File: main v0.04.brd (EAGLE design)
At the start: 77.5 x 67.3 mm, 70 parts, among them IC1 4050D, U1 MCP73831, U2 TPS61200, U3 MAX1704X, U4 USD-SOCKETNEW, X1 USB-MICROB, Y1 16MHz KX-7

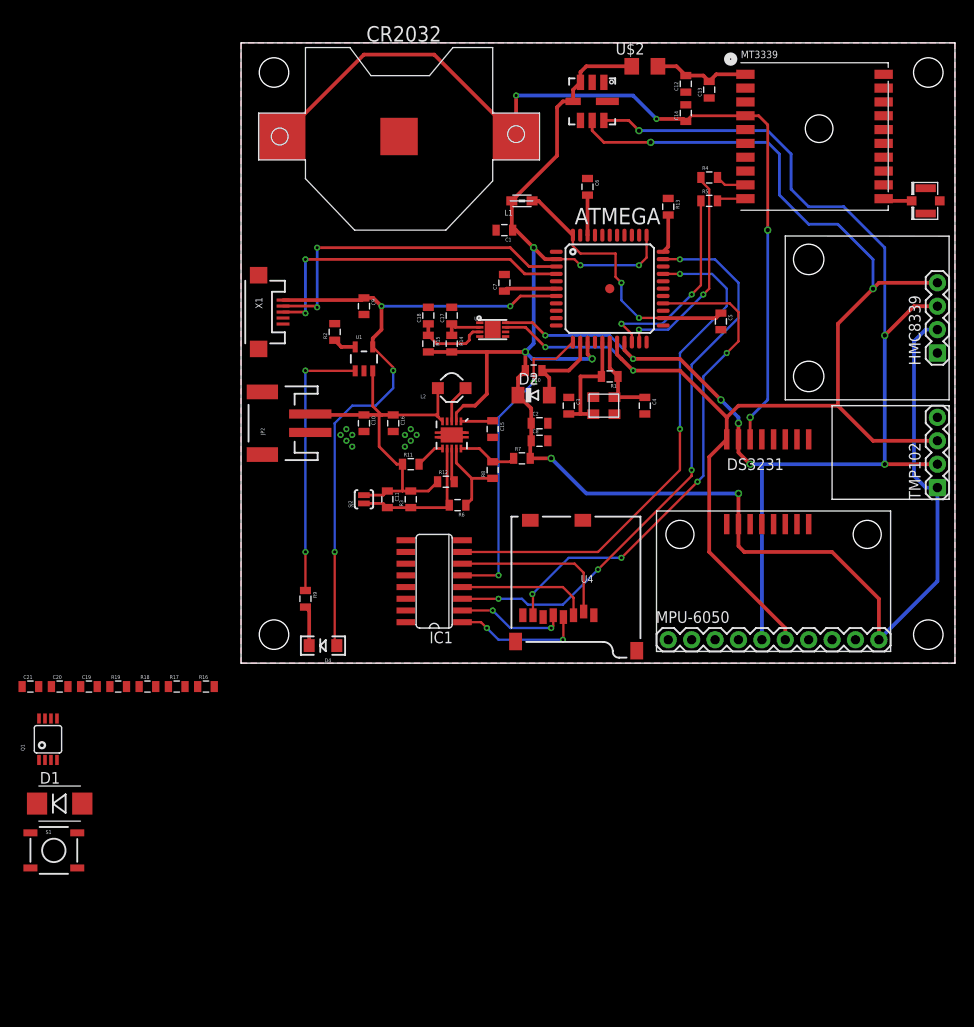
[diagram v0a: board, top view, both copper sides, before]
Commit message: Clean up of schematics
General clean up + 5V reg added + On/off control connected
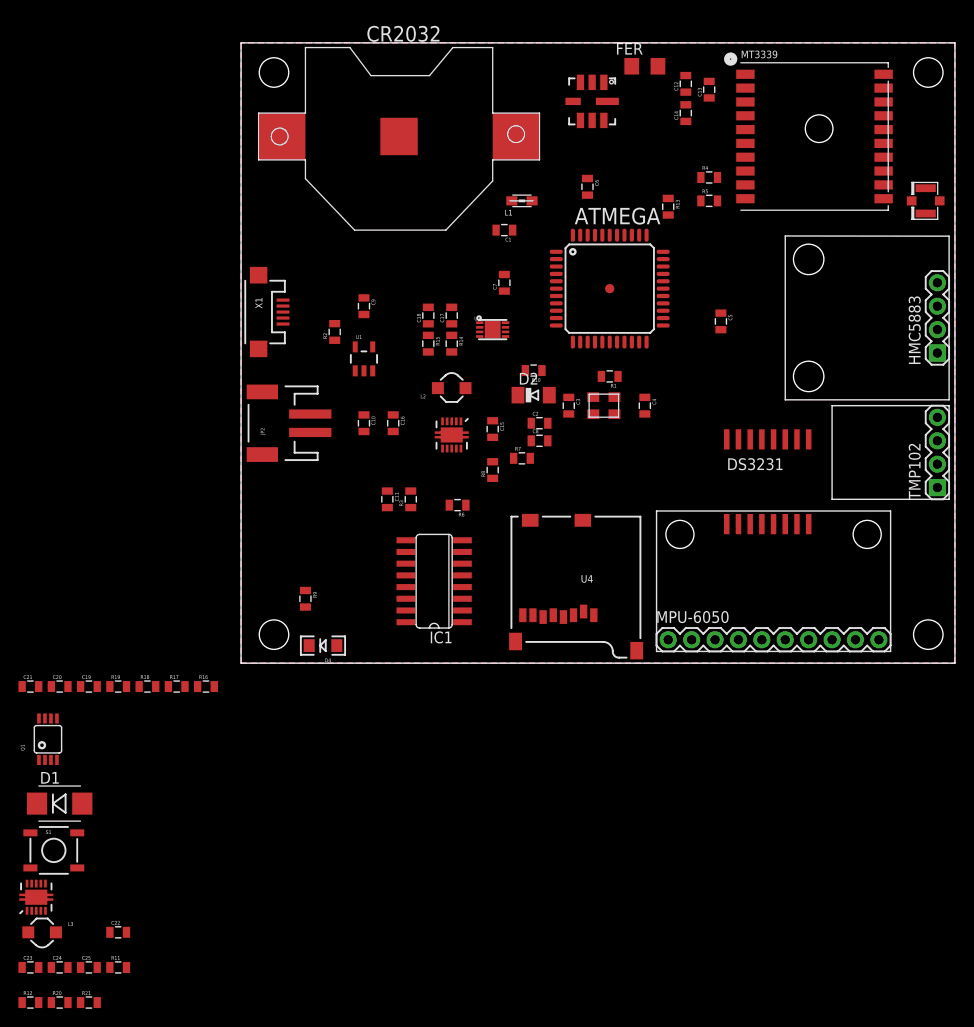
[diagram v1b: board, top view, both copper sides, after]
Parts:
- removed SJ2: UVLO Disable, SparkFun-Passives:SJ_2S-NO
- added C22: 22uF, SparkFun:0805
- added C23, C24: 0.1uF, SparkFun:0805
- added C25: 10uF, SparkFun:0805
- added L3: 4.7uH, 1.2A, SparkFun:CDRH2D09
- added R20: 2M, SparkFun:0805
- added R21: 220k, SparkFun:0805
- added U5: TPS61200, SparkFun:QFN-10_PAD
- R11: value 10k -> 2M
- R12: value 10k -> 220k
- moved R12 72.3 mm to (-22.9, -36.8)
- moved R11 63.2 mm to (-13.3, -33.0)
- renumbered HMC8339 to HMC5883, U$2 to FER
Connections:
- removed net EN: R11.2, U2.6
- removed net N$22: C21.2, Q1.3, R19.2
- removed net PS: R12.2, U2.8
- removed net VBAT: C20.2, Q1.5, Q1.6, R16.2, R17.2
- removed net VBATT: C10.1, C11.1, C16.1, JP2.2, L2.P$2, R11.1, R12.1, R3.2, SJ2.2, U1.3, U2.5
- new net 5V: C22.1, R20.2, U5.2
- new net EN5V: U5.6
- new net N$16: L3.P$1, U5.3
- new net N$17: C24.1, U5.1
- new net UVLO1: C23.2, R11.1, R12.2, U5.7
- new net VIN: C11.1, C16.1, C21.2, C23.1, C25.1, L2.P$2, L3.P$2, Q1.3, R11.2, R19.2, R3.2, U2.5, U2.6, U2.8, U5.5, U5.8
- new net V_BATT: C10.1, C20.2, JP2.2, Q1.5, Q1.6, R14.2, R15.2, R16.2, R17.2, U1.3
- net AUX_SCL: now also HMC5883.4
- net AUX_SDA: now also HMC5883.3
- net FB: now also R20.1, R21.2, U5.10
- net GND: now also C22.2, C24.2, C25.2, U5.11, U5.12, U5.13, U5.14, U5.15, U5.4
- net GND1: now also R12.1, R21.1, U5.9
- net SCL: no longer HMC5883.4
- net SDA: no longer HMC5883.3
- net UVLO: no longer SJ2.1
- net VCC: no longer R14.2, R15.2
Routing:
- net VCC: track 191.4 -> 0.00 mm, vias 7 -> 0
- net SCL: track 149.8 -> 0.00 mm, vias 4 -> 0
- net SDA: track 145.7 -> 0.00 mm, vias 8 -> 0
- net VEE: track 101.3 -> 0.00 mm, vias 4 -> 0
- net VUSB: track 73.1 -> 0.00 mm, vias 4 -> 0
- net IO13*: track 63.2 -> 0.00 mm, vias 4 -> 0
- net IO10*: track 56.6 -> 0.00 mm, vias 2 -> 0
- net IO12: track 54.1 -> 0.00 mm, vias 4 -> 0
- net VBATT: track 41.3 -> 0.00 mm
- net RD-: track 37.0 -> 0.00 mm, vias 2 -> 0
- net RD+: track 36.2 -> 0.00 mm, vias 2 -> 0
- net IO11*: track 34.0 -> 0.00 mm, vias 2 -> 0
- net N$14: track 29.3 -> 0.00 mm, vias 2 -> 0
- net AVCC: track 29.3 -> 0.00 mm, vias 2 -> 0
- net TX: track 23.3 -> 0.00 mm, vias 2 -> 0
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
